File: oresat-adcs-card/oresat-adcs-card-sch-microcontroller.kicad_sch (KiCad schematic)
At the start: 23 parts, among them U14 TCAN330GDCNT, U15 STM32F042K6T7, X2 ECS-160-10-36Q-ES-TR

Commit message: Design review changes
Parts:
- added TP49, TP56, TP59: Test-Point, OreSat-TestPoint:1X01, symbol OreSat-TestPoint:Test-Point
- C28, C29, C30, C36, C37, C38, C39, R11, R12, R7, R8, R9: footprint (none) -> oresat-acs-card:.0603-C-NOSILK
- D2: footprint (none) -> oresat-acs-card:LED-0603
- J2: value (none) -> ORESAT-DEBUG-CONNECTOR-SOLAR; footprint (none) -> oresat-footprints:J-TE_2-1734592-0
- TP10, TP11, TP12, TP13, TP14, TP9: value (none) -> TEST-POINT-LARGE-SQUARE; footprint (none) -> oresat-acs-card:1X01
- U14: footprint (none) -> oresat-acs-card:SOT23-8_TI-DCN
- U15: footprint (none) -> oresat-acs-card:STM32F091C
- X2: footprint (none) -> oresat-acs-card:CRYSTAL_2.5X2
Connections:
- net at U15.2 (PC13): now also TP49.1
- net at U15.3 (PC14-OSC32_IN): now also TP56.1
- net at U15.4 (PC15-OSC32_OUT): now also TP59.1
- net MT_FAULT renamed MT_EN/~{FAULT}
- no-connect marks 0 -> 4
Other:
- note removed: "NOTE: PB6 and PB7 tied together via 2x 10k resistors @ MAX7310~{}"

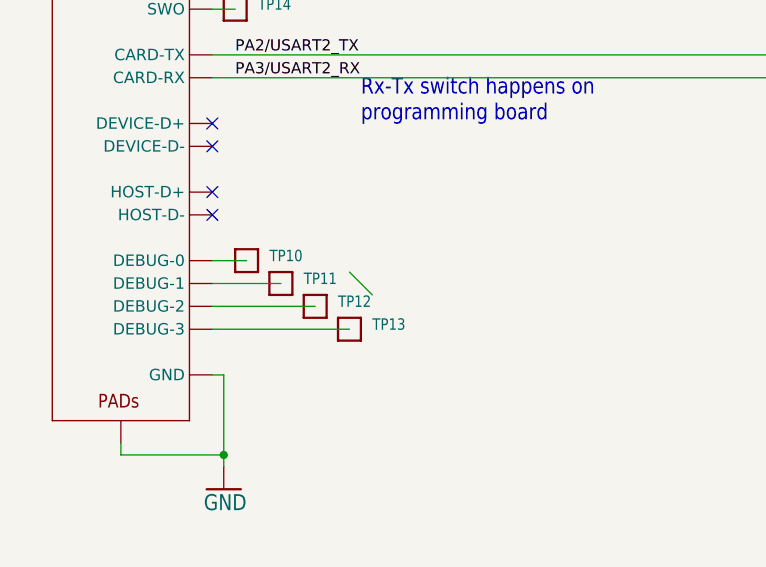
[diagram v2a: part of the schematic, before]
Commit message: Updated MT OPD breaker current limiting, and added OPD addresses to schematic
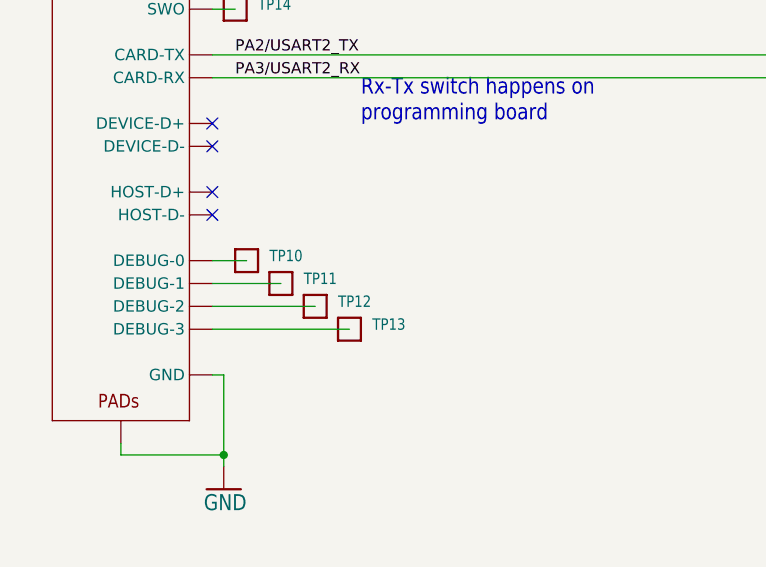
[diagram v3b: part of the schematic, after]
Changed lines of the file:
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@@
   (no_connect (at 39.37 200.66))
   (no_connect (at 39.37 198.12))
-  (bus_entry (at 54.61 214.63) (size 2.54 2.54)
-    (stroke (width 0) (type default) (color 0 0 0 0))
-  )
   (wire (pts (xy 63.5 88.9) (xy 63.5 86.36))
     (stroke (width 0) (type default) (color 0 0 0 0))

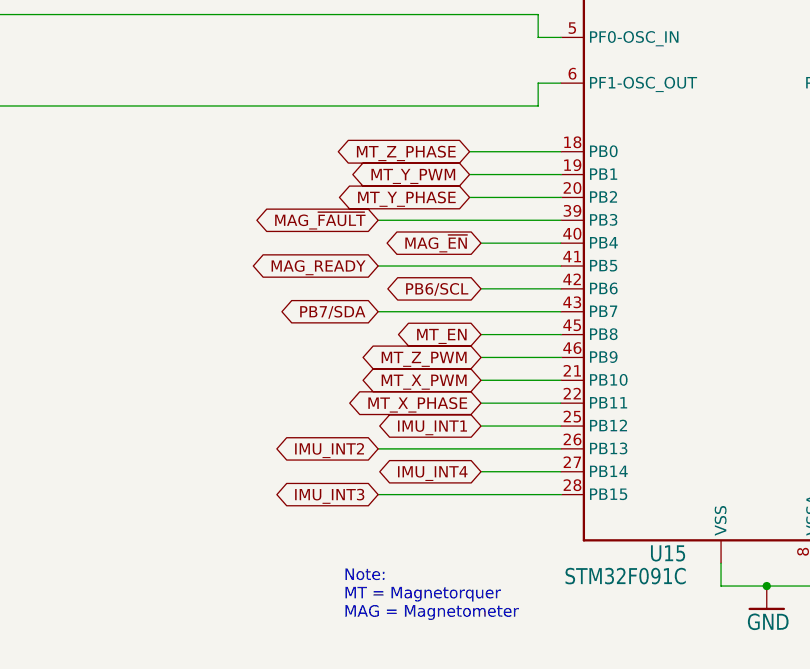
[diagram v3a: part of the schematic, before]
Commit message: Fixed ADCS card issues
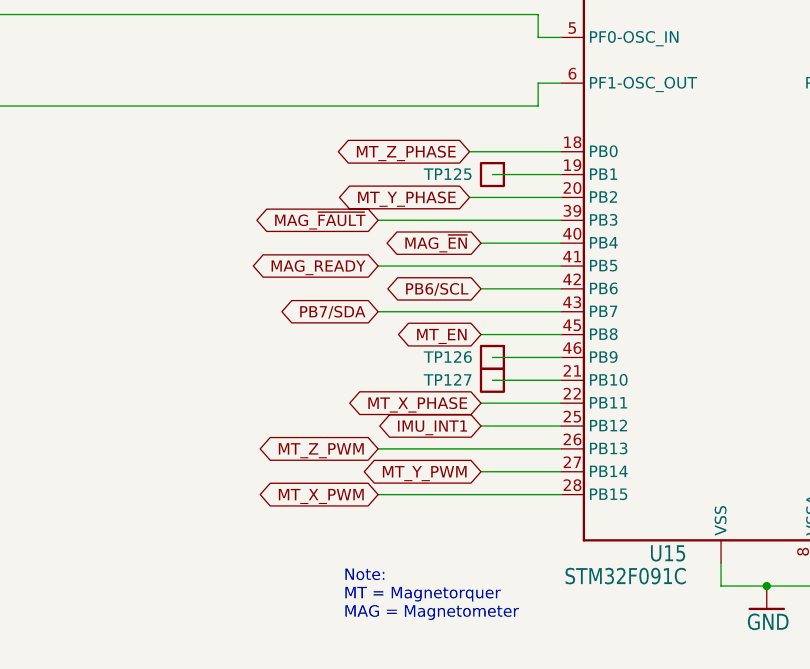
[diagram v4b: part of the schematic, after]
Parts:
- added TP125, TP126, TP127: Test-Point, OreSat-TestPoint:1X01, symbol OreSat-TestPoint:Test-Point
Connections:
- net IMU_INT2 is gone; now on net MT_Z_PWM: U15.26 (PB13)
- net IMU_INT3 is gone; now on net MT_X_PWM: U15.28 (PB15)
- net IMU_INT4 is gone; now on net MT_Y_PWM: U15.27 (PB14)
- net MT_X_PWM: no longer U15.21 (PB10)
- net MT_Y_PWM: no longer U15.19 (PB1)
- net MT_Z_PWM: no longer U15.46 (PB9)
- new net: TP127.1, U15.21 (PB10)
- new net: TP126.1, U15.46 (PB9)
- new net: TP125.1, U15.19 (PB1)
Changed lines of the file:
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@@
     (stroke (width 0) (type default) (color 0 0 0 0))
   )
-  (wire (pts (xy 181.61 106.68) (xy 190.5 106.68))
+  (wire (pts (xy 182.88 106.68) (xy 190.5 106.68))
     (stroke (width 0) (type default) (color 0 0 0 0))
   )
@@
     (stroke (width 0) (type default) (color 0 0 0 0))
   )
-  (wire (pts (xy 180.34 86.36) (xy 190.5 86.36))
+  (wire (pts (xy 182.88 86.36) (xy 190.5 86.36))
     (stroke (width 0) (type default) (color 0 0 0 0))
   )
@@
     (stroke (width 0) (type default) (color 0 0 0 0))
   )
-  (wire (pts (xy 181.61 109.22) (xy 190.5 109.22))
-    (stroke (width 0) (type default) (color 0 0 0 0))
-  )
   (wire (pts (xy 39.37 175.26) (xy 50.8 175.26))
     (stroke (width 0) (type default) (color 0 0 0 0))
@@
   )
   (wire (pts (xy 289.56 190.5) (xy 39.37 190.5))
+    (stroke (width 0) (type default) (color 0 0 0 0))
+  )
+  (wire (pts (xy 182.88 109.22) (xy 190.5 109.22))
     (stroke (width 0) (type default) (color 0 0 0 0))
   )
@@
     (effects (font (size 1.2446 1.2446)) (justify left bottom))
   )
-  (global_label "MT_X_PWM" (shape bidirectional) (at 181.61 109.22 180) (fields_autoplaced)
+  (global_label "MT_X_PWM" (shape bidirectional) (at 170.18 121.92 180) (fields_autoplaced)
     (effects (font (size 1.27 1.27)) (justify right))
-    (property "Intersheet References" "${INTERSHEET_REFS}" (id 0) (at 169.0369 109.1406 0)
+    (property "Intersheet References" "${INTERSHEET_REFS}" (id 0) (at 157.6069 121.8406 0)
       (effects (font (size 1.27 1.27)) (justify right) hide)
     )
@@
     )
   )
-  (global_label "IMU_INT3" (shape bidirectional) (at 170.18 121.92 180) (fields_autoplaced)
-    (effects (font (size 1.2446 1.2446)) (justify right))
-    (property "Intersheet References" "${INTERSHEET_REFS}" (id 0) (at 299.72 -322.58 0)
-      (effects (font (size 1.27 1.27)) hide)
-    )
-  )
   (global_label "CAN_TX" (shape input) (at 259.08 121.92 270) (fields_autoplaced)
     (effects (font (size 1.2446 1.2446)) (justify right))
@@
     )
   )
-  (global_label "MT_Y_PWM" (shape bidirectional) (at 180.34 86.36 180) (fields_autoplaced)
+  (global_label "MT_Y_PWM" (shape bidirectional) (at 181.61 119.38 180) (fields_autoplaced)
     (effects (font (size 1.27 1.27)) (justify right))
-    (property "Intersheet References" "${INTERSHEET_REFS}" (id 0) (at 167.8879 86.2806 0)
+    (property "Intersheet References" "${INTERSHEET_REFS}" (id 0) (at 169.1579 119.3006 0)
       (effects (font (size 1.27 1.27)) (justify right) hide)
     )
@@
     (property "Intersheet References" "${INTERSHEET_REFS}" (id 0) (at 269.1622 138.6273 90)
       (effects (font (size 1.2446 1.2446)) (justify right) hide)
-    )
-  )
-  (global_label "IMU_INT4" (shape bidirectional) (at 181.61 119.38 180) (fields_autoplaced)
-    (effects (font (size 1.2446 1.2446)) (justify right))
-    (property "Intersheet References" "${INTERSHEET_REFS}" (id 0) (at 334.01 -327.66 0)
-      (effects (font (size 1.27 1.27)) hide)
     )
   )
@@
     )
   )
-  (global_label "MT_Z_PWM" (shape bidirectional) (at 181.61 106.68 180) (fields_autoplaced)
+  (global_label "MT_Z_PWM" (shape bidirectional) (at 170.18 116.84 180) (fields_autoplaced)
     (effects (font (size 1.27 1.27)) (justify right))
-    (property "Intersheet References" "${INTERSHEET_REFS}" (id 0) (at 169.0369 106.6006 0)
+    (property "Intersheet References" "${INTERSHEET_REFS}" (id 0) (at 157.6069 116.7606 0)
       (effects (font (size 1.27 1.27)) (justify right) hide)
     )
@@
     )
   )
-  (global_label "IMU_INT2" (shape bidirectional) (at 170.18 116.84 180) (fields_autoplaced)
-    (effects (font (size 1.2446 1.2446)) (justify right))
-    (property "Intersheet References" "${INTERSHEET_REFS}" (id 0) (at 299.72 -332.74 0)
-      (effects (font (size 1.27 1.27)) hide)
-    )
-  )
   (global_label "MT_ILIM" (shape input) (at 256.54 93.98 0) (fields_autoplaced)
     (effects (font (size 1.27 1.27)) (justify left))
@@
     (pin "1")
     (pin "2")
+  )
+  (symbol (lib_id "OreSat-TestPoint:Test-Point") (at 182.88 109.22 270) (unit 1)
+    (in_bom yes) (on_board yes)
+    (property "Reference" "TP127" (id 0) (at 175.26 109.22 90)
+      (effects (font (size 1.27 1.27)) (justify left))
+    )
+    (property "Value" "Test-Point" (id 1) (at 185.42 109.22 0)
+      (effects (font (size 1.27 1.27)) hide)
+    )
+    (property "Footprint" "OreSat-TestPoint:1X01" (id 2) (at 185.42 109.22 0)
+      (effects (font (size 1.27 1.27)) hide)
+    )
+    (property "Datasheet" "" (id 3) (at 185.42 109.22 0)
+      (effects (font (size 1.27 1.27)) hide)
+    )
+    (pin "1")
   )
   (symbol (lib_id "oresat-acs-card-eagle-import:TCAN330") (at 368.3 109.22 0) (unit 1)
@@
     (pin "1")
   )
+  (symbol (lib_id "OreSat-TestPoint:Test-Point") (at 182.88 106.68 270) (unit 1)
+    (in_bom yes) (on_board yes)
+    (property "Reference" "TP126" (id 0) (at 175.26 106.68 90)
+      (effects (font (size 1.27 1.27)) (justify left))
+    )
+    (property "Value" "Test-Point" (id 1) (at 185.42 106.68 0)
+      (effects (font (size 1.27 1.27)) hide)
+    )
+    (property "Footprint" "OreSat-TestPoint:1X01" (id 2) (at 185.42 106.68 0)
+      (effects (font (size 1.27 1.27)) hide)
+    )
+    (property "Datasheet" "" (id 3) (at 185.42 106.68 0)
+      (effects (font (size 1.27 1.27)) hide)
+    )
+    (pin "1")
+  )
   (symbol (lib_id "oresat-acs-card-eagle-import:GND") (at 200.66 40.64 0) (unit 1)
     (in_bom yes) (on_board yes)
@@
       (effects (font (size 1.27 1.27)) hide)
     )
+    (pin "1")
+  )
+  (symbol (lib_id "OreSat-TestPoint:Test-Point") (at 182.88 86.36 270) (unit 1)
+    (in_bom yes) (on_board yes)
+    (property "Reference" "TP125" (id 0) (at 175.26 86.36 90)
+      (effects (font (size 1.27 1.27)) (justify left))
+    )
+    (property "Value" "Test-Point" (id 1) (at 185.42 86.36 0)
+      (effects (font (size 1.27 1.27)) hide)
+    )
+    (property "Footprint" "OreSat-TestPoint:1X01" (id 2) (at 185.42 86.36 0)
+      (effects (font (size 1.27 1.27)) hide)
+    )
+    (property "Datasheet" "" (id 3) (at 185.42 86.36 0)
+      (effects (font (size 1.27 1.27)) hide)
+    )
